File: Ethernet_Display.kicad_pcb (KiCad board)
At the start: 2 copper layers, 67.1 x 53.3 mm, 9 parts, among them J1 Power, J2 Analog, J4 Digital, J5 Digital, J6 Conn_01x16, P6 CONN_01X01, P8 CONN_01X01

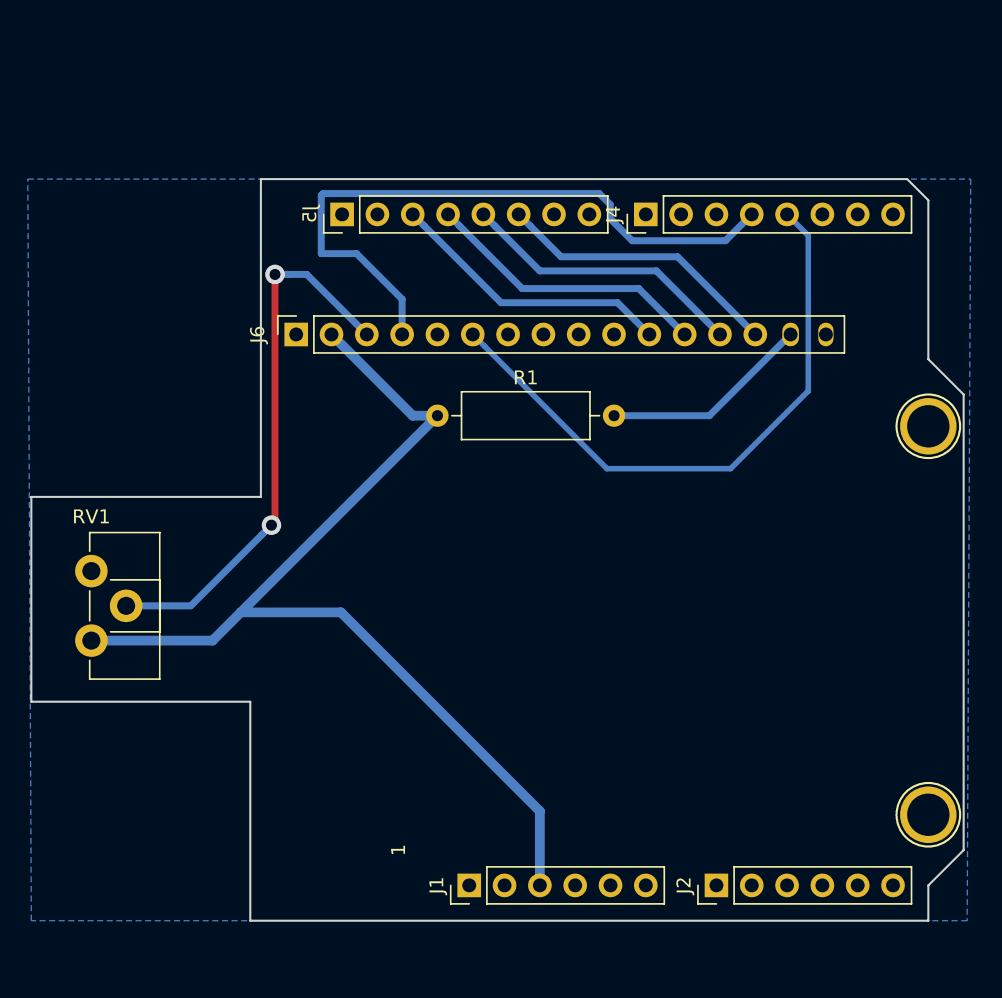
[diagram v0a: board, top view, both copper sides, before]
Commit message: Fixup wrong wiring
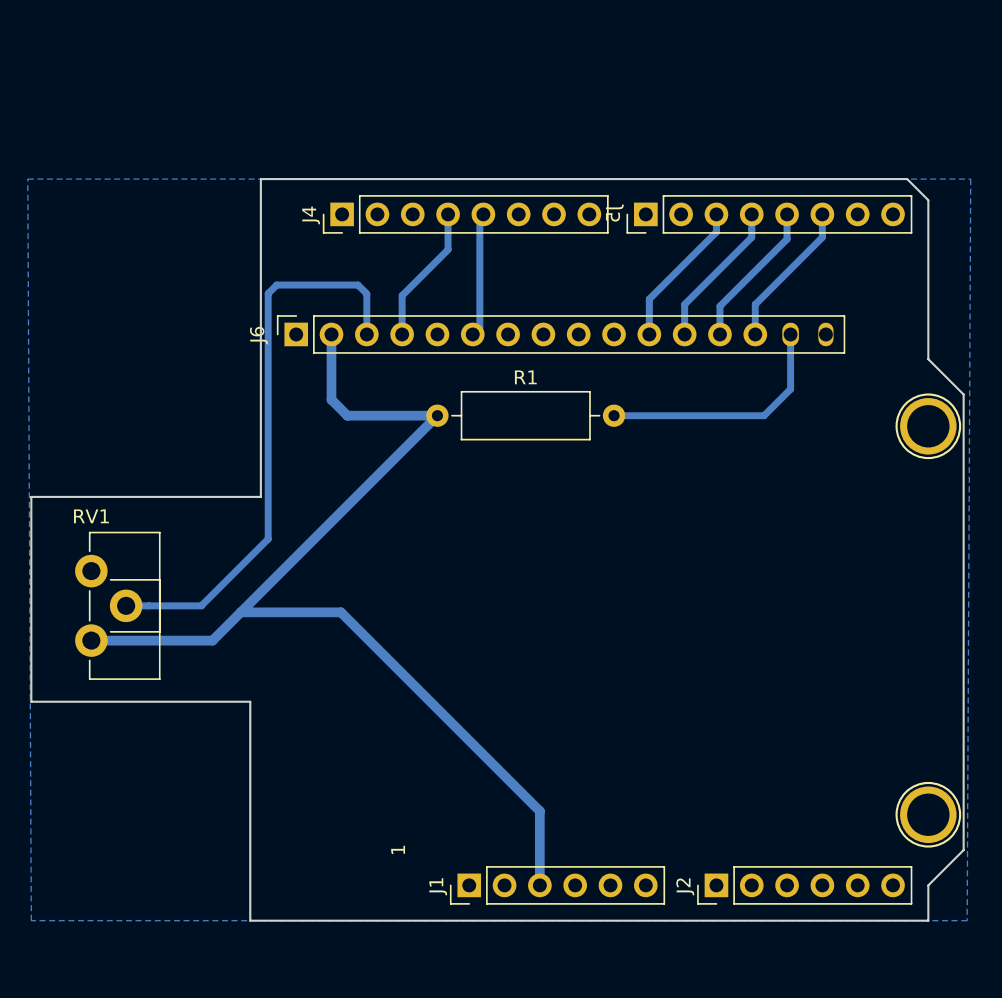
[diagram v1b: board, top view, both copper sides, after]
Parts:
- moved J4 21.8 mm to (42.2, 18.9)
- moved J5 21.8 mm to (64.0, 18.9)
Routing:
- net D12: track 47.7 -> 10.0 mm
- net D11: track 43.8 -> 8.95 mm
- net D4: track 20.6 -> 10.8 mm
- net D2: track 20.6 -> 10.8 mm
- net D5: track 20.6 -> 10.8 mm
- net D3: track 20.6 -> 10.8 mm
- net +5V: track 74.4 -> 77.2 mm
- net Net-(J6-Pad15): track 15.1 -> 17.4 mm
- net Net-(J6-Pad3): track 39.4 -> 40.4 mm, vias 2 -> 0

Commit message: new version
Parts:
- added LED1: LED, LED_THT:LED_D3.0mm_Horizontal_O3.81mm_Z2.0mm, F.Cu at (40.4, 14.7)
- added R2: 100, Resistor_THT:R_Axial_DIN0309_L9.0mm_D3.2mm_P12.70mm_Horizontal, F.Cu at (66.0, 14.7)
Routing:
- net Net-(LED1-Pad1): track 0.00 -> 25.7 mm
- net D9: track 0.00 -> 23.2 mm
- net GND: track 0.00 -> 18.7 mm, vias 0 -> 2
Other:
- board size 67.1 x 53.3 mm -> 67.2 x 58.8 mm
- net class Default: trace_width 0.5 -> 1.016
